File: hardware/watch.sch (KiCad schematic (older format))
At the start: 1 part, among them J1 DX07S016JA1R1500

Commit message: modified bom
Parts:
- J1: MNR (none) -> DX07S016JA1R1500
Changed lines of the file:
@@
 F 4 "JAE Electronics" H 3200 3750 50  0001 C CNN "Manufacturer"
 F 5 "https://www.mouser.at/ProductDetail/JAE-Electronics/DX07S016JA1R1500?qs=%2Fha2pyFaduhIxG%252BJ4XjlZeX%2FOvIg0QPAOjcqMfE5RQ7WfL0OkHc3Zw%3D%3D" H 3200 3750 50  0001 C CNN "Order"
+F 6 "DX07S016JA1R1500" H 3200 3750 50  0001 C CNN "MNR"
 	1    3200 3750
 	1    0    0    -1

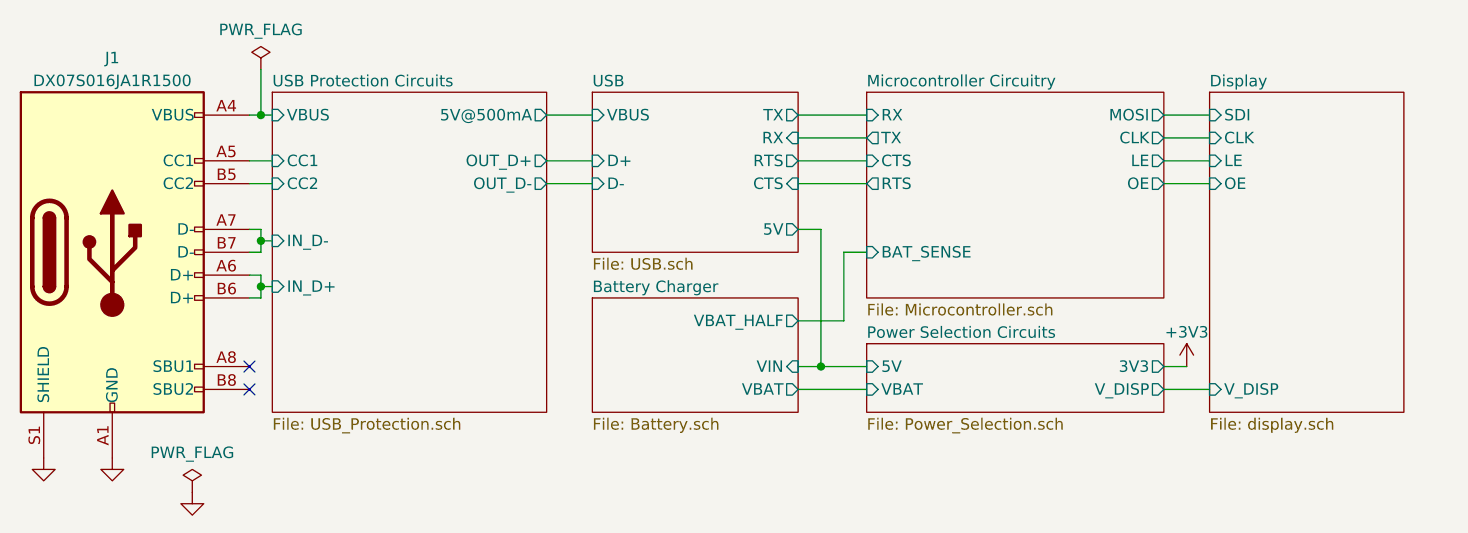
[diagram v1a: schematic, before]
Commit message: New uC, ditched FTDI chip, and more!
Need to improve the schematic a little bit more.
For example, I want to be able to turn the LED Drivers off using
a MOSFET.

For the PCB Layout: I want to move as many components as possible
to the top layer, so that they are visible when in the case.
Also, I have to consider solderability of the components, the more
complex should all be on one layer for easier soldering.

Next up: Finishing the schematic, improving component placement,
and routing!
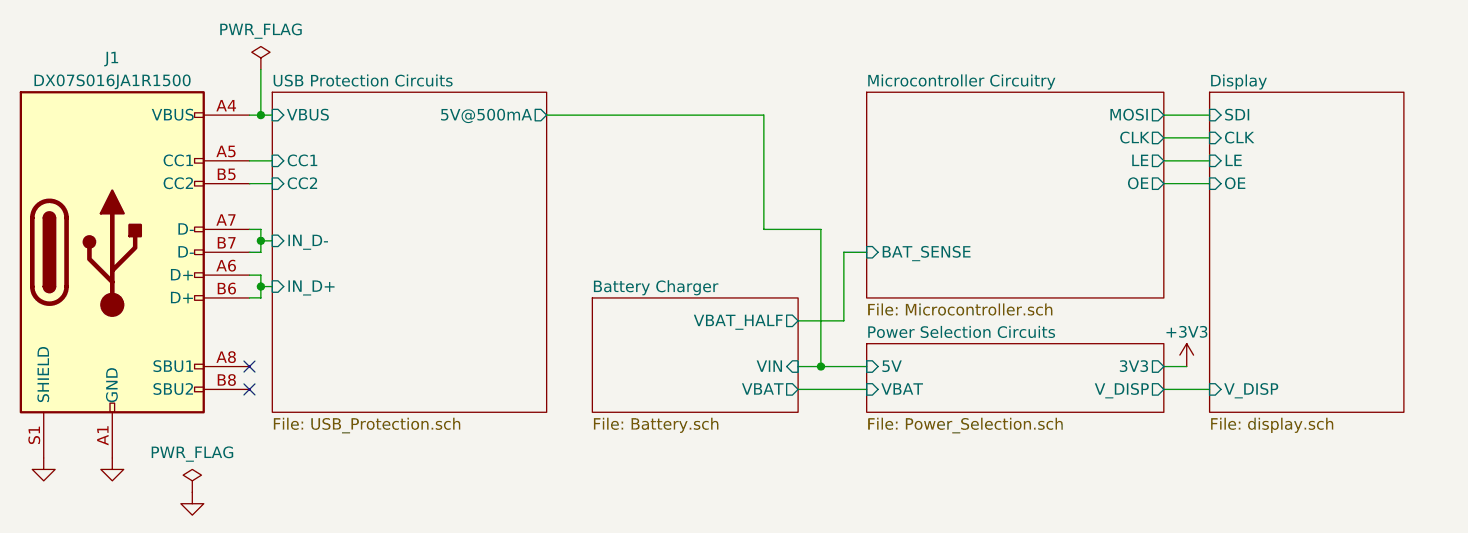
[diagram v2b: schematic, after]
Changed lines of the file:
@@
 $Descr A4 11693 8268
 encoding utf-8
-Sheet 1 7
+Sheet 1 6
 Title "aWristWatch"
 Date "2021-04-05"
@@
 F6 "IN_D+" I L 3900 3900 50
 F7 "IN_D-" I L 3900 3700 50
-F8 "OUT_D+" O R 5100 3350 50
-F9 "OUT_D-" O R 5100 3450 50
 $EndSheet
 $Sheet
@@
 F4 "V_DISP" O R 7800 4350 50
 F5 "3V3" O R 7800 4250 50
-$EndSheet
-$Sheet
-S 6500 3050 1300 900
-U 605DA130
-F0 "Microcontroller Circuitry" 50
-F1 "Microcontroller.sch" 50
-F2 "LE" O R 7800 3350 50
-F3 "CLK" O R 7800 3250 50
-F4 "MOSI" O R 7800 3150 50
-F5 "OE" O R 7800 3450 50
-F6 "BAT_SENSE" I L 6500 3750 50
-F7 "TX" O L 6500 3250 50
-F8 "RX" I L 6500 3150 50
-F9 "CTS" I L 6500 3350 50
-F10 "RTS" O L 6500 3450 50
 $EndSheet
 Wire Wire Line
@@
 	1    0    0    -1
 $EndComp
-$Sheet
-S 5300 3050 900  700
-U 605F7522
-F0 "USB" 50
-F1 "USB.sch" 50
-F2 "VBUS" I L 5300 3150 50
-F3 "D+" I L 5300 3350 50
-F4 "D-" I L 5300 3450 50
-F5 "5V" O R 6200 3650 50
-F6 "TX" O R 6200 3150 50
-F7 "RTS" O R 6200 3350 50
-F8 "RX" I R 6200 3250 50
-F9 "CTS" I R 6200 3450 50
-$EndSheet
 Wire Wire Line
 	3800 3650 3850 3650
@@
 	3850 3900 3850 3950
 Wire Wire Line
-	5300 3150 5100 3150
-Wire Wire Line
-	5100 3450 5300 3450
-Wire Wire Line
-	5300 3350 5100 3350
-Wire Wire Line
-	6200 3650 6300 3650
-Wire Wire Line
 	6300 3650 6300 4250
 Wire Wire Line
@@
 	6300 4250 6500 4250
 Connection ~ 6300 4250
-Wire Wire Line
-	6200 3450 6500 3450
-Wire Wire Line
-	6500 3350 6200 3350
-Wire Wire Line
-	6200 3250 6500 3250
-Wire Wire Line
-	6500 3150 6200 3150
 Wire Wire Line
 	7800 3150 8000 3150
@@
 	1    0    0    -1
 $EndComp
+Wire Wire Line
+	6050 3150 6050 3650
+Wire Wire Line
+	5100 3150 6050 3150
+Wire Wire Line
+	6050 3650 6300 3650
+$Sheet
+S 6500 3050 1300 900
+U 605DA130
+F0 "Microcontroller Circuitry" 50
+F1 "Microcontroller.sch" 50
+F2 "LE" O R 7800 3350 50
+F3 "CLK" O R 7800 3250 50
+F4 "MOSI" O R 7800 3150 50
+F5 "OE" O R 7800 3450 50
+F6 "BAT_SENSE" I L 6500 3750 50
+$EndSheet
 $EndSCHEMATC

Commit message: Updated to KiCad v6.0
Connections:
- net USB Protection Circuits/IN_D+: no longer names the net of J1.A6 (D+)
- net USB Protection Circuits/IN_D+: no longer J1.B6 (D+)
- net USB Protection Circuits/IN_D-: no longer names the net of J1.A7 (D-)
- net USB Protection Circuits/IN_D-: no longer J1.B7 (D-)
- no-connect marks 2 -> 6
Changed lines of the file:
@@
 $EndDescr
 $Sheet
-S 8000 3050 850  1400
+S 8200 3050 850  1400
 U 60633D5C
 F0 "Display" 50
 F1 "display.sch" 50
-F2 "SDI" I L 8000 3150 50
-F3 "CLK" I L 8000 3250 50
-F4 "LE" I L 8000 3350 50
-F5 "OE" I L 8000 3450 50
-F6 "V_DISP" I L 8000 4350 50
+F2 "SDI" I L 8200 3400 50
+F3 "CLK" I L 8200 3500 50
+F4 "LE" I L 8200 3600 50
+F5 "OE" I L 8200 3700 50
+F6 "POWER_IN" I L 8200 3150 50
 $EndSheet
 $Comp
@@
 F4 "CC2" I L 3900 3450 50
 F5 "5V@500mA" O R 5100 3150 50
-F6 "IN_D+" I L 3900 3900 50
-F7 "IN_D-" I L 3900 3700 50
 $EndSheet
 $Sheet
-S 5300 3950 900  500
+S 5400 3950 1200 500
 U 6063DAC2
 F0 "Battery Charger" 50
 F1 "Battery.sch" 50
-F2 "VIN" I R 6200 4250 50
-F3 "VBAT" O R 6200 4350 50
-F4 "VBAT_HALF" O R 6200 4050 50
+F2 "VIN" I L 5400 4150 50
+F3 "VBAT" O L 5400 4050 50
+F4 "VBAT_HALF" O R 6600 4050 50
 $EndSheet
 $Sheet
-S 6500 4150 1300 300
+S 5400 3050 1200 700
 U 605CEFBE
 F0 "Power Selection Circuits" 50
 F1 "Power_Selection.sch" 50
-F2 "5V" I L 6500 4250 50
-F3 "VBAT" I L 6500 4350 50
-F4 "V_DISP" O R 7800 4350 50
-F5 "3V3" O R 7800 4250 50
+F2 "5V" I L 5400 3150 50
+F3 "VBAT" I L 5400 3250 50
+F4 "V_DISP" O R 6600 3150 50
+F5 "VuC" O R 6600 3400 50
+F6 "LED_CTRL" I R 6600 3500 50
 $EndSheet
 Wire Wire Line
@@
 	1    0    0    -1
 $EndComp
-Wire Wire Line
-	3800 3650 3850 3650
-Wire Wire Line
-	3850 3650 3850 3700
-Wire Wire Line
-	3850 3750 3800 3750
-Wire Wire Line
-	3800 3850 3850 3850
-Wire Wire Line
-	3850 3850 3850 3900
-Wire Wire Line
-	3850 3950 3800 3950
-Wire Wire Line
-	3900 3700 3850 3700
-Connection ~ 3850 3700
-Wire Wire Line
-	3850 3700 3850 3750
-Wire Wire Line
-	3850 3900 3900 3900
-Connection ~ 3850 3900
-Wire Wire Line
-	3850 3900 3850 3950
-Wire Wire Line
-	6300 3650 6300 4250
-Wire Wire Line
-	6300 4250 6200 4250
-Wire Wire Line
-	6200 4050 6400 4050
-Wire Wire Line
-	6400 4050 6400 3750
-Wire Wire Line
-	6400 3750 6500 3750
-Wire Wire Line
-	6200 4350 6500 4350
-Wire Wire Line
-	6300 4250 6500 4250
-Connection ~ 6300 4250
-Wire Wire Line
-	7800 3150 8000 3150
-Wire Wire Line
-	8000 3250 7800 3250
-Wire Wire Line
-	7800 3350 8000 3350
-Wire Wire Line
-	8000 3450 7800 3450
-Wire Wire Line
-	7800 4350 8000 4350
-$Comp
-L power:+3V3 #PWR0101
-U 1 1 60611A17
-P 7900 4250
-F 0 "#PWR0101" H 7900 4100 50  0001 C CNN
-F 1 "+3V3" H 7900 4400 50  0000 C CNN
-F 2 "" H 7900 4250 50  0001 C CNN
-F 3 "" H 7900 4250 50  0001 C CNN
-	1    7900 4250
-	1    0    0    -1
-$EndComp
-Wire Wire Line
-	7900 4250 7800 4250
 $Comp
 L power:PWR_FLAG #FLG0101
@@
 	1    0    0    -1
 $EndComp
-Wire Wire Line
-	6050 3150 6050 3650
-Wire Wire Line
-	5100 3150 6050 3150
-Wire Wire Line
-	6050 3650 6300 3650
 $Sheet
-S 6500 3050 1300 900
+S 6750 3300 1300 1150
 U 605DA130
 F0 "Microcontroller Circuitry" 50
 F1 "Microcontroller.sch" 50
-F2 "LE" O R 7800 3350 50
-F3 "CLK" O R 7800 3250 50
-F4 "MOSI" O R 7800 3150 50
-F5 "OE" O R 7800 3450 50
-F6 "BAT_SENSE" I L 6500 3750 50
+F2 "LE" O R 8050 3600 50
+F3 "CLK" O R 8050 3500 50
+F4 "MOSI" O R 8050 3400 50
+F5 "OE" O R 8050 3700 50
+F6 "BAT_SENSE" I L 6750 4050 50
+F7 "LED_POWER_CTL" O L 6750 3500 50
 $EndSheet
+NoConn ~ 3800 3650
+NoConn ~ 3800 3750
+NoConn ~ 3800 3850
+NoConn ~ 3800 3950
+Wire Wire Line
+	5400 4050 5300 4050
+Wire Wire Line
+	5400 4150 5200 4150
+Wire Wire Line
+	5100 3150 5200 3150
+Wire Wire Line
+	8200 3150 6600 3150
+Wire Wire Line
+	8050 3400 8200 3400
+Wire Wire Line
+	8200 3500 8050 3500
+Wire Wire Line
+	8050 3600 8200 3600
+Wire Wire Line
+	8200 3700 8050 3700
+Wire Wire Line
+	6750 3500 6600 3500
+Wire Wire Line
+	5300 3250 5400 3250
+Wire Wire Line
+	5300 3250 5300 4050
+Wire Wire Line
+	5200 3150 5200 4150
+Connection ~ 5200 3150
+Wire Wire Line
+	5200 3150 5400 3150
+Wire Wire Line
+	6750 4050 6600 4050
 $EndSCHEMATC
